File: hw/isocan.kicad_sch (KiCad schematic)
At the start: 18 parts, among them U10 ISO6521F, U12 TJA1051TK/3,118, U6 MIE1W0505BGLVH-3R-Z, U9 ISO6521FREUR

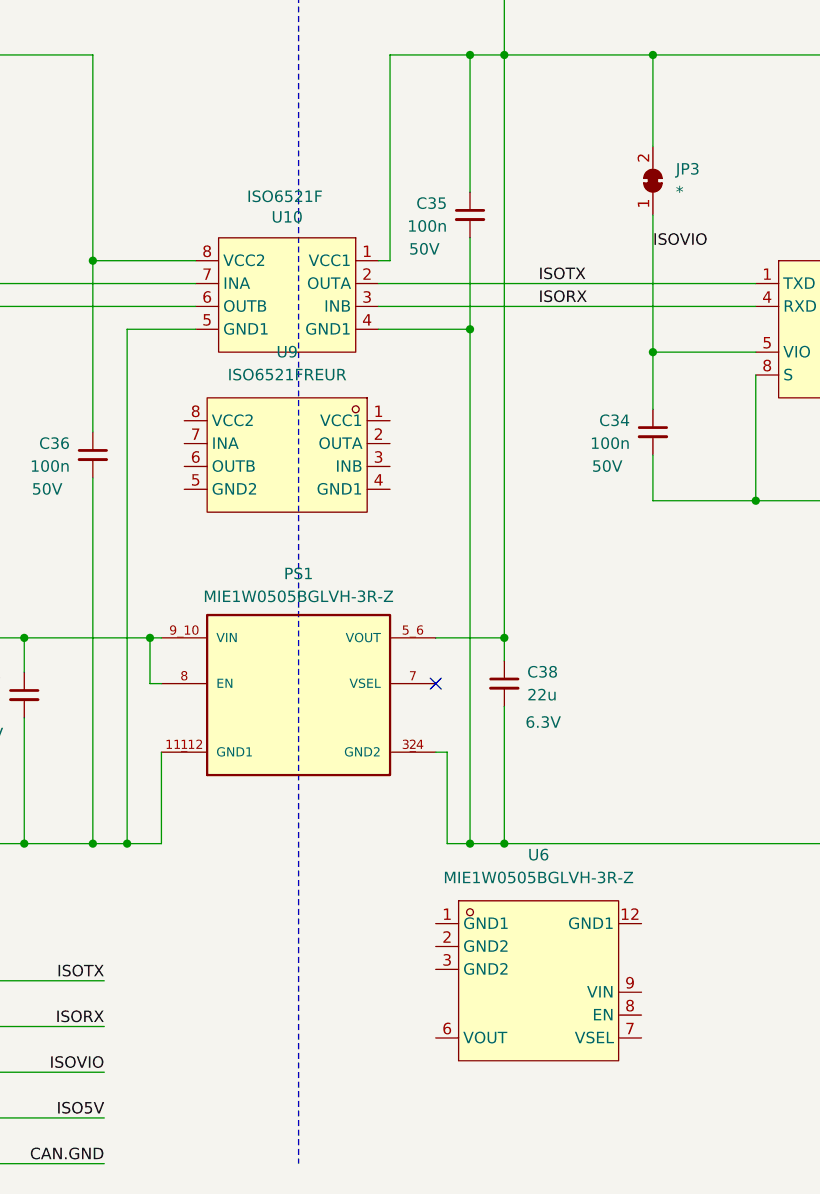
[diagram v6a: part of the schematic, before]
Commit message: [Hw] Rerouted for timer swap, usb replaced, hall pullups topside, silk version
Signed-off-by: Will Haarhoff <williamhaarhoff@gmail.com>
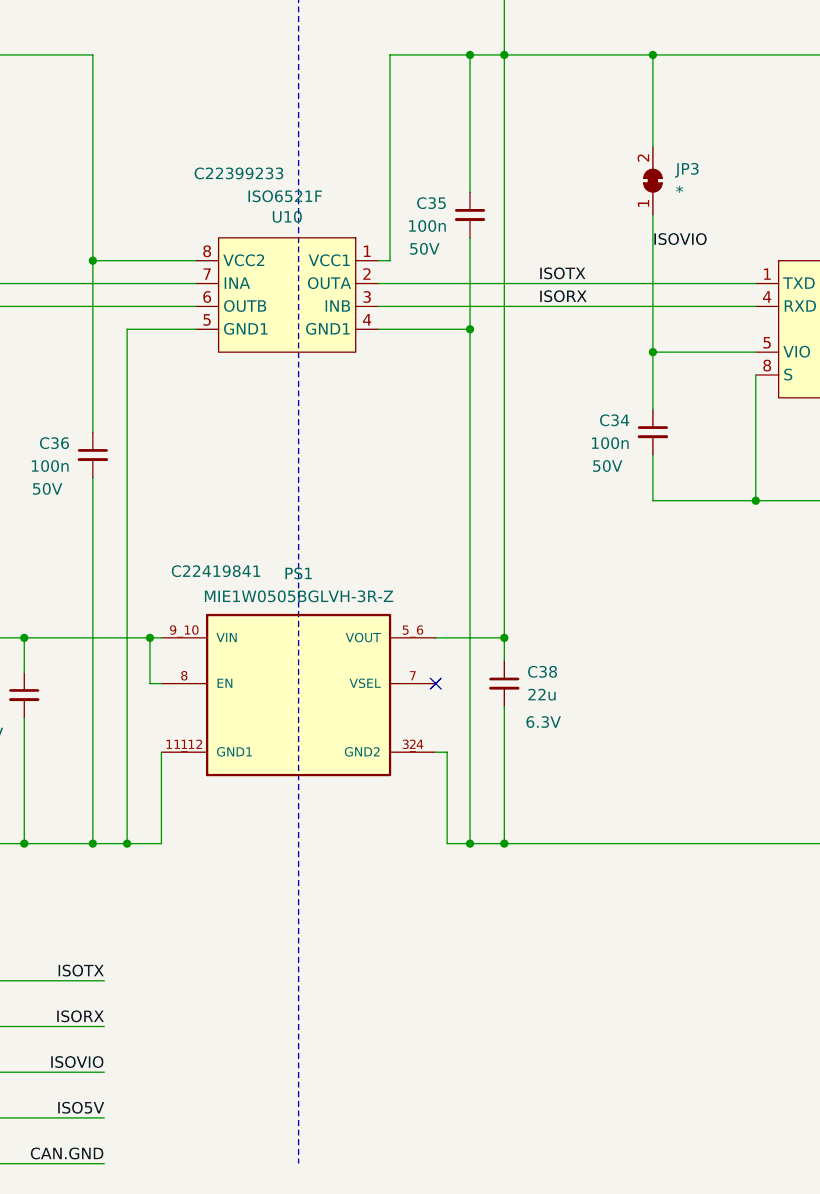
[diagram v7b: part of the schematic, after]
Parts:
- removed U6: MIE1W0505BGLVH-3R-Z, easyeda:LGA-12_L4.0-W5.0_MIE1W0505BGLVH, symbol easyeda:MIE1W0505BGLVH-3R-Z
- removed U9: ISO6521FREUR, easyeda:XSON-8_L3.0-W2.0-P0.50-BL, symbol easyeda:ISO6521FREUR
- PS1: LCSC (none) -> C22419841
- U10: LCSC (none) -> C22399233
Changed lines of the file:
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@@
+			)
+		)
+		(property "LCSC" "C22419841"
+			(at 87.376 104.394 0)
+			(effects
+				(font
+					(size 1.27 1.27)
+				)
 			)
 		)
@@
 				(path "/6a0f293a-1ae1-497a-a3c1-0d8f9e6f81b9/67c38edc-7843-4b4c-b50a-94fd700c0fa2"
 					(reference "PS1")
-					(unit 1)
-				)
-			)
-		)
-	)
-	(symbol
-		(lib_id "easyeda:MIE1W0505BGLVH-3R-Z")
-		(at 123.19 149.86 0)
-		(unit 1)
-		(exclude_from_sim no)
-		(in_bom yes)
-		(on_board yes)
-		(dnp no)
-		(fields_autoplaced yes)
-		(property "Reference" "U6"
-			(at 123.19 135.89 0)
-			(effects
-				(font
-					(size 1.27 1.27)
-				)
-			)
-		)
-		(property "Value" "MIE1W0505BGLVH-3R-Z"
-			(at 123.19 138.43 0)
-			(effects
-				(font
-					(size 1.27 1.27)
-				)
-			)
-		)
-		(property "Footprint" "easyeda:LGA-12_L4.0-W5.0_MIE1W0505BGLVH"
-			(at 123.19 163.83 0)
-			(effects
-				(font
-					(size 1.27 1.27)
-				)
-				(hide yes)
-			)
-		)
-		(property "Datasheet" ""
-			(at 123.19 149.86 0)
-			(effects
-				(font
-					(size 1.27 1.27)
-				)
-				(hide yes)
-			)
-		)
-		(property "Description" ""
-			(at 123.19 149.86 0)
-			(effects
-				(font
-					(size 1.27 1.27)
-				)
-				(hide yes)
-			)
-		)
-		(property "LCSC Part" "C22419841"
-			(at 123.19 166.37 0)
-			(effects
-				(font
-					(size 1.27 1.27)
-				)
-				(hide yes)
-			)
-		)
-		(pin "1"
-		)
-		(pin "6"
-		)
-		(pin "12"
-		)
-		(pin "3"
-		)
-		(pin "7"
-		)
-		(pin "9"
-		)
-		(pin "8"
-		)
-		(pin "2"
-		)
-		(instances
-			(project ""
-				(path "/6a0f293a-1ae1-497a-a3c1-0d8f9e6f81b9/67c38edc-7843-4b4c-b50a-94fd700c0fa2"
-					(reference "U6")
 					(unit 1)
 				)
@@
 				(path "/6a0f293a-1ae1-497a-a3c1-0d8f9e6f81b9/67c38edc-7843-4b4c-b50a-94fd700c0fa2"
 					(reference "JP6")
-					(unit 1)
-				)
-			)
-		)
-	)
-	(symbol
-		(lib_id "easyeda:ISO6521FREUR")
-		(at 95.25 91.44 0)
-		(mirror y)
-		(unit 1)
-		(exclude_from_sim no)
-		(in_bom yes)
-		(on_board yes)
-		(dnp no)
-		(fields_autoplaced yes)
-		(property "Reference" "U9"
-			(at 95.25 80.01 0)
-			(effects
-				(font
-					(size 1.27 1.27)
-				)
-			)
-		)
-		(property "Value" "ISO6521FREUR"
-			(at 95.25 82.55 0)
-			(effects
-				(font
-					(size 1.27 1.27)
-				)
-			)
-		)
-		(property "Footprint" "easyeda:XSON-8_L3.0-W2.0-P0.50-BL"
-			(at 95.25 102.87 0)
-			(effects
-				(font
-					(size 1.27 1.27)
-				)
-				(hide yes)
-			)
-		)
-		(property "Datasheet" ""
-			(at 95.25 91.44 0)
-			(effects
-				(font
-					(size 1.27 1.27)
-				)
-				(hide yes)
-			)
-		)
-		(property "Description" ""
-			(at 95.25 91.44 0)
-			(effects
-				(font
-					(size 1.27 1.27)
-				)
-				(hide yes)
-			)
-		)
-		(property "LCSC Part" "C22399233"
-			(at 95.25 105.41 0)
-			(effects
-				(font
-					(size 1.27 1.27)
-				)
-				(hide yes)
-			)
-		)
-		(pin "7"
-		)
-		(pin "6"
-		)
-		(pin "5"
-		)
-		(pin "3"
-		)
-		(pin "4"
-		)
-		(pin "8"
-		)
-		(pin "1"
-		)
-		(pin "2"
-		)
-		(instances
-			(project ""
-				(path "/6a0f293a-1ae1-497a-a3c1-0d8f9e6f81b9/67c38edc-7843-4b4c-b50a-94fd700c0fa2"
-					(reference "U9")
 					(unit 1)
 				)
@@
 			)
 		)
+		(property "LCSC" "C22399233"
+			(at 89.916 60.198 0)
+			(effects
+				(font
+					(size 1.27 1.27)
+				)
+			)
+		)

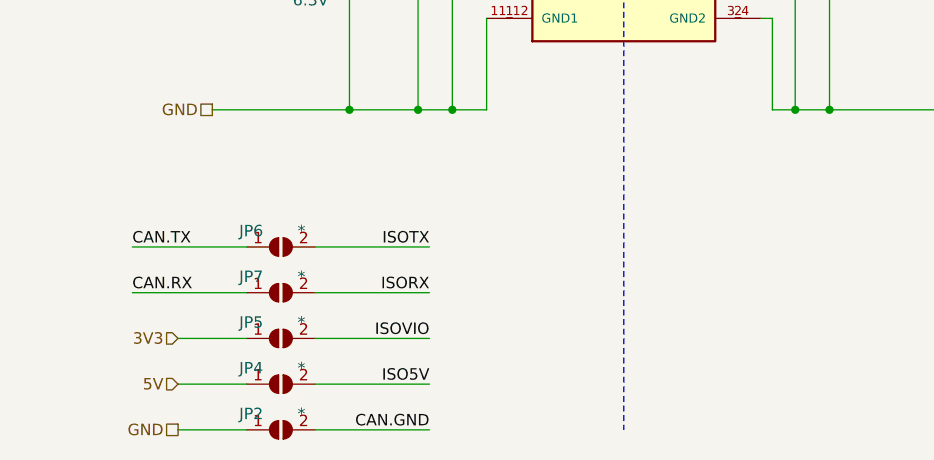
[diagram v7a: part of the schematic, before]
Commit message: [Hw] Cleaned up schematic, 10m isense shunts, green power led, DRC
Signed-off-by: Will Haarhoff <williamhaarhoff@gmail.com>
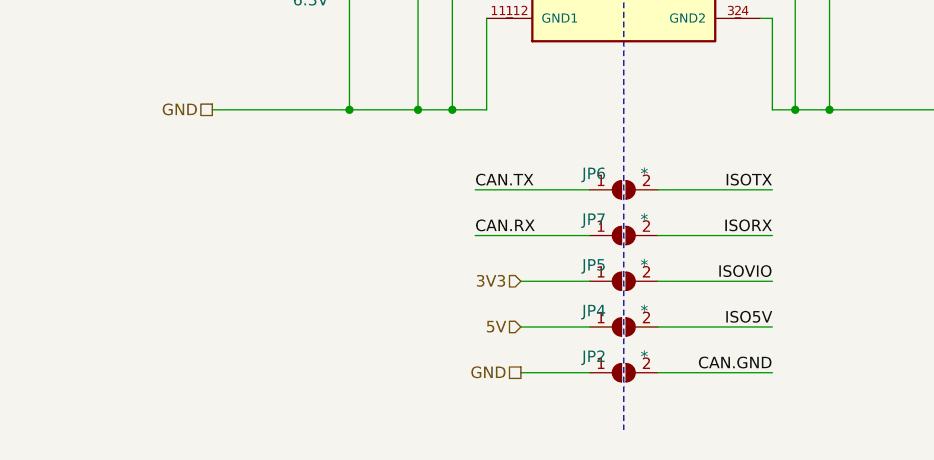
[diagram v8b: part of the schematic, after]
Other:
- moved on the sheet: JP2, JP4, JP5, JP6, JP7
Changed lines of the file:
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@@
 	(wire
 		(pts
-			(xy 74.93 170.18) (xy 62.23 170.18)
-		)
-		(stroke
-			(width 0)
-			(type default)
-		)
-	)
-	(wire
-		(pts
-			(xy 62.23 149.86) (xy 74.93 149.86)
+			(xy 113.03 163.83) (xy 100.33 163.83)
+		)
+		(stroke
+			(width 0)
+			(type default)
+		)
+	)
+	(wire
+		(pts
+			(xy 100.33 143.51) (xy 113.03 143.51)
 		)
 		(stroke
@@
 	(wire
 		(pts
-			(xy 54.61 154.94) (xy 41.91 154.94)
+			(xy 92.71 148.59) (xy 80.01 148.59)
 		)
 		(stroke
@@
 	(wire
 		(pts
-			(xy 46.99 170.18) (xy 54.61 170.18)
+			(xy 85.09 163.83) (xy 92.71 163.83)
 		)
 		(stroke
@@
 	(wire
 		(pts
-			(xy 62.23 165.1) (xy 74.93 165.1)
+			(xy 100.33 158.75) (xy 113.03 158.75)
 		)
 		(stroke
@@
 	(wire
 		(pts
-			(xy 54.61 149.86) (xy 41.91 149.86)
+			(xy 92.71 143.51) (xy 80.01 143.51)
 		)
 		(stroke
@@
 	(wire
 		(pts
-			(xy 62.23 160.02) (xy 74.93 160.02)
+			(xy 100.33 153.67) (xy 113.03 153.67)
 		)
 		(stroke
@@
 	(wire
 		(pts
-			(xy 46.99 165.1) (xy 54.61 165.1)
+			(xy 85.09 158.75) (xy 92.71 158.75)
 		)
 		(stroke
@@
 	(wire
 		(pts
-			(xy 62.23 154.94) (xy 74.93 154.94)
+			(xy 100.33 148.59) (xy 113.03 148.59)
 		)
 		(stroke
@@
 	(wire
 		(pts
-			(xy 46.99 160.02) (xy 54.61 160.02)
+			(xy 85.09 153.67) (xy 92.71 153.67)
 		)
 		(stroke
@@
 	)
 	(label "CAN.RX"
-		(at 41.91 154.94 0)
+		(at 80.01 148.59 0)
 		(effects
 			(font
@@
 	)
 	(label "ISORX"
-		(at 74.93 154.94 180)
+		(at 113.03 148.59 180)
 		(effects
 			(font
@@
 	)
 	(label "ISOVIO"
-		(at 74.93 160.02 180)
+		(at 113.03 153.67 180)
 		(effects
 			(font
@@
 	)
 	(label "ISO5V"
-		(at 74.93 165.1 180)
+		(at 113.03 158.75 180)
 		(effects
 			(font
@@
 	)
 	(label "CAN.TX"
-		(at 41.91 149.86 0)
+		(at 80.01 143.51 0)
 		(effects
 			(font
@@
 	)
 	(label "CAN.GND"
-		(at 74.93 170.18 180)
+		(at 113.03 163.83 180)
 		(effects
 			(font
@@
 	)
 	(label "ISOTX"
-		(at 74.93 149.86 180)
+		(at 113.03 143.51 180)
 		(effects
 			(font
@@
 	(hierarchical_label "GND"
 		(shape passive)
-		(at 46.99 170.18 180)
+		(at 85.09 163.83 180)
 		(effects
 			(font
@@
 	(hierarchical_label "5V"
 		(shape input)
-		(at 46.99 165.1 180)
+		(at 85.09 158.75 180)
 		(effects
 			(font
@@
 	(hierarchical_label "3V3"
 		(shape input)
-		(at 46.99 160.02 180)
+		(at 85.09 153.67 180)
 		(effects
 			(font
@@
 	(symbol
 		(lib_id "Jumper:SolderJumper_2_Open")
-		(at 58.42 149.86 0)
+		(at 96.52 143.51 0)
 		(unit 1)
 		(exclude_from_sim no)
@@
 		(dnp no)
 		(property "Reference" "JP6"
-			(at 55.118 148.082 0)
+			(at 93.218 141.732 0)
 			(effects
 				(font
@@
 		)
 		(property "Value" "*"
-			(at 60.706 148.082 0)
+			(at 98.806 141.732 0)
 			(effects
 				(font
@@
 		)
 		(property "Footprint" "local_lib:jumper12_open"
-			(at 58.42 149.86 0)
+			(at 96.52 143.51 0)
 			(effects
 				(font
@@
 		)
 		(property "Datasheet" "~"
-			(at 58.42 149.86 0)
+			(at 96.52 143.51 0)
 			(effects
 				(font
@@
 		)
 		(property "Description" ""
-			(at 58.42 149.86 0)
+			(at 96.52 143.51 0)
 			(effects
 				(font
@@
 	(symbol
 		(lib_id "Jumper:SolderJumper_2_Open")
-		(at 58.42 154.94 0)
+		(at 96.52 148.59 0)
 		(unit 1)
 		(exclude_from_sim no)
@@
 		(dnp no)
 		(property "Reference" "JP7"
-			(at 55.118 153.162 0)
+			(at 93.218 146.812 0)
 			(effects
 				(font
@@
 		)
 		(property "Value" "*"
-			(at 60.706 153.162 0)
+			(at 98.806 146.812 0)
 			(effects
 				(font
@@
 		)
 		(property "Footprint" "local_lib:jumper12_open"
-			(at 58.42 154.94 0)
+			(at 96.52 148.59 0)
 			(effects
 				(font
@@
 		)
 		(property "Datasheet" "~"
-			(at 58.42 154.94 0)
+			(at 96.52 148.59 0)
 			(effects
 				(font
@@
 		)
 		(property "Description" ""
-			(at 58.42 154.94 0)
+			(at 96.52 148.59 0)
 			(effects
 				(font
@@
 	(symbol
 		(lib_id "Jumper:SolderJumper_2_Open")
-		(at 58.42 170.18 0)
+		(at 96.52 163.83 0)
 		(unit 1)
 		(exclude_from_sim no)
@@
 		(dnp no)
 		(property "Reference" "JP2"
-			(at 55.118 168.402 0)
+			(at 93.218 162.052 0)
 			(effects
 				(font
@@
 		)
 		(property "Value" "*"
-			(at 60.706 168.402 0)
+			(at 98.806 162.052 0)
 			(effects
 				(font
@@
 		)
 		(property "Footprint" "local_lib:jumper12_open"
-			(at 58.42 170.18 0)
+			(at 96.52 163.83 0)
 			(effects
 				(font
@@
 		)
 		(property "Datasheet" "~"
-			(at 58.42 170.18 0)
+			(at 96.52 163.83 0)
 			(effects
 				(font
@@
 		)
 		(property "Description" ""
-			(at 58.42 170.18 0)
+			(at 96.52 163.83 0)
 			(effects
 				(font
@@
 	(symbol
 		(lib_id "Jumper:SolderJumper_2_Open")
-		(at 58.42 160.02 0)
+		(at 96.52 153.67 0)
 		(unit 1)
 		(exclude_from_sim no)
@@
 		(dnp no)
 		(property "Reference" "JP5"
-			(at 55.118 158.242 0)
+			(at 93.218 151.892 0)
 			(effects
 				(font
@@
 		)
 		(property "Value" "*"
-			(at 60.706 158.242 0)
+			(at 98.806 151.892 0)
 			(effects
 				(font
@@
 		)
 		(property "Footprint" "local_lib:jumper12_open"
-			(at 58.42 160.02 0)
+			(at 96.52 153.67 0)
 			(effects
 				(font
@@
 		)
 		(property "Datasheet" "~"
-			(at 58.42 160.02 0)
+			(at 96.52 153.67 0)
 			(effects
 				(font
@@
 		)
 		(property "Description" ""
-			(at 58.42 160.02 0)
+			(at 96.52 153.67 0)
 			(effects
 				(font
@@
 	(symbol
 		(lib_id "Jumper:SolderJumper_2_Open")
-		(at 58.42 165.1 0)
+		(at 96.52 158.75 0)
 		(unit 1)
 		(exclude_from_sim no)
@@
 		(dnp no)
 		(property "Reference" "JP4"
-			(at 55.118 163.322 0)
+			(at 93.218 156.972 0)
 			(effects
 				(font
@@
 		)
 		(property "Value" "*"
-			(at 60.706 163.322 0)
+			(at 98.806 156.972 0)
 			(effects
 				(font
@@
 		)
 		(property "Footprint" "local_lib:jumper12_open"
-			(at 58.42 165.1 0)
+			(at 96.52 158.75 0)
 			(effects
 				(font
@@
 		)
 		(property "Datasheet" "~"
-			(at 58.42 165.1 0)
+			(at 96.52 158.75 0)
 			(effects
 				(font
@@
 		)
 		(property "Description" ""
-			(at 58.42 165.1 0)
-			(effects
-				(font
+			(at 96.52 158.75 0)
+			(effects
+				(font
